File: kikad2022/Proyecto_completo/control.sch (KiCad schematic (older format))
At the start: 33 parts, among them IC2 LM393AD, IC3 74HC02PW,112, J1 Conn_01x02_Male, J10 Conn_01x01_Male, J2 Conn_01x01_Male, J4 Conn_01x01_Male, J5 Conn_01x01_Male, J6 Conn_01x01_Male, J7 Conn_01x01_Male, J9 Conn_01x01_Male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

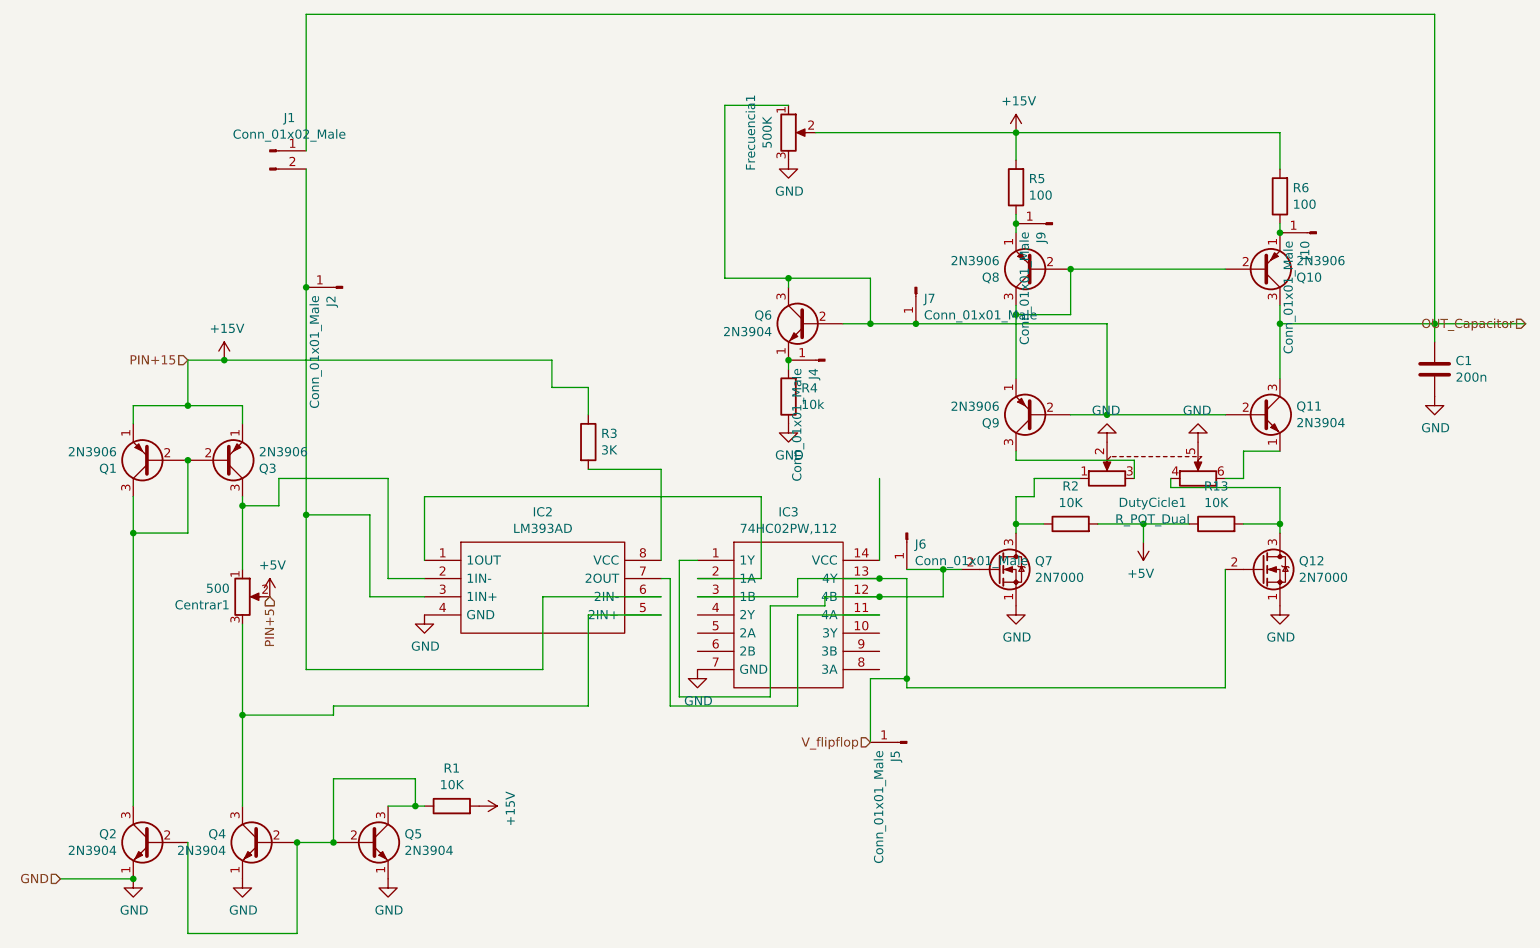
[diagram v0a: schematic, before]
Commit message: kikad_modificaciones
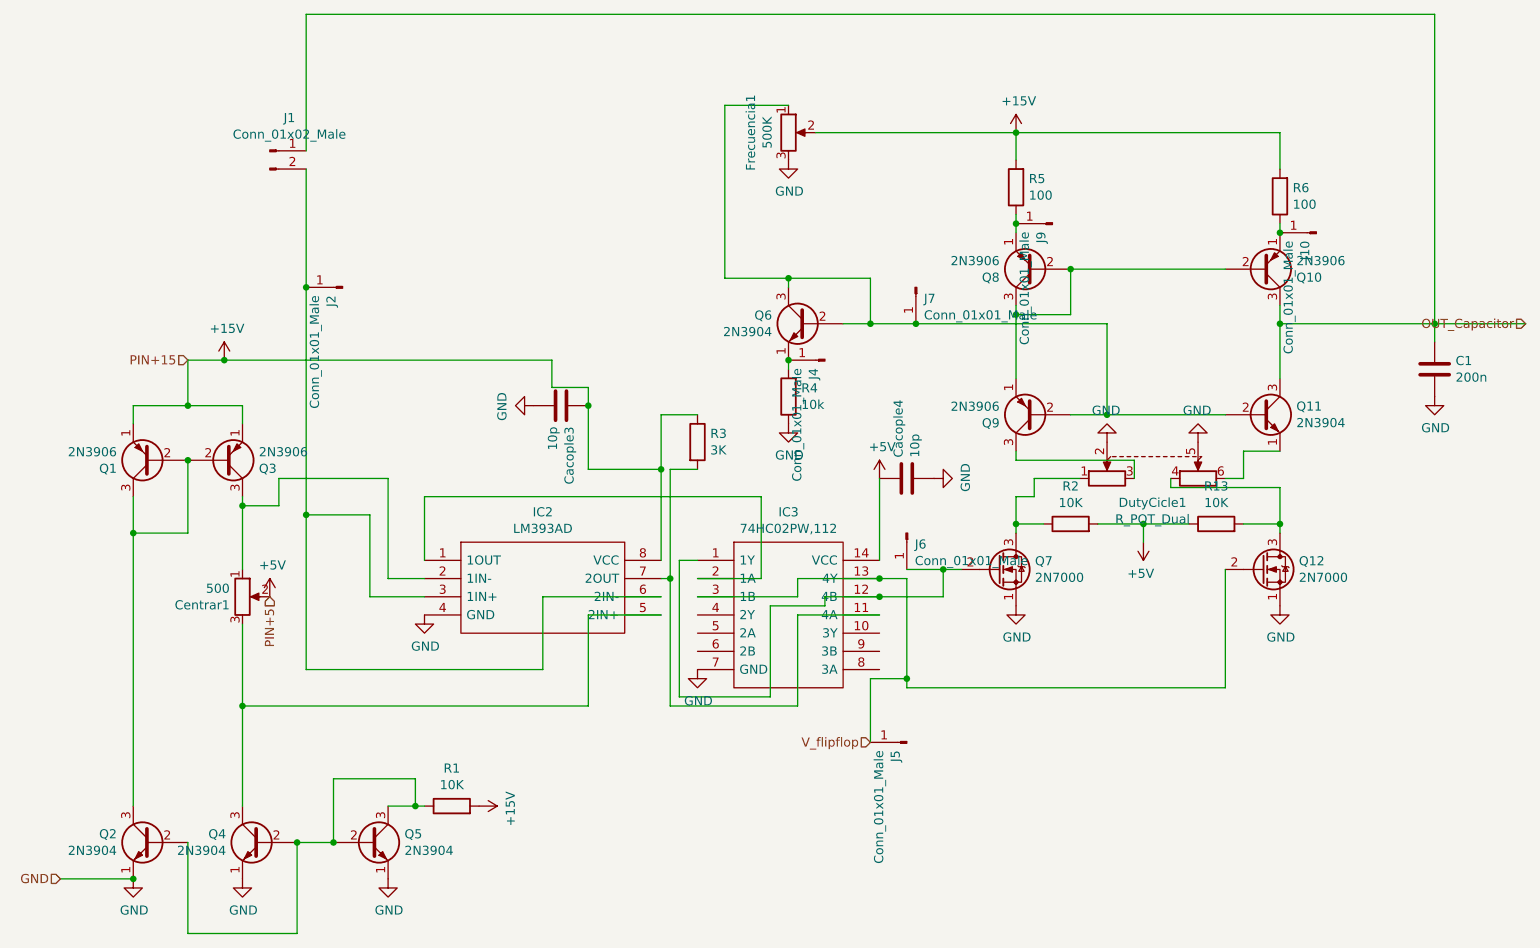
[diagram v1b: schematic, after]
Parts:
- added Cacople3, Cacople4: 10p, Capacitor_SMD:C_0603_1608Metric, symbol Device:C
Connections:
- net +15V: now also IC2.8 (VCC), Cacople3.2
- net +5V: now also IC3.14 (VCC), Cacople4.2
- net GND: now also Cacople3.1, Cacople4.1
- net at R3.2: now also IC2.7 (2OUT), IC3.11 (4A); no longer IC2.8 (VCC)
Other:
- moved on the sheet: R3
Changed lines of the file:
@@
 Connection ~ 3350 3850
 Connection ~ 3950 3700
-Wire Wire Line
-	3950 4850 4450 4850
-Wire Wire Line
-	4450 4850 4450 4800
 $Comp
 L Device:R R3
 U 1 1 61FADEA7
-P 5850 3350
-F 0 "R3" H 5920 3396 50  0000 L CNN
-F 1 "3K" H 5920 3305 50  0000 L CNN
-F 2 "Resistor_SMD:R_0603_1608Metric" V 5780 3350 50  0001 C CNN
-F 3 "~" H 5850 3350 50  0001 C CNN
-	1    5850 3350
+P 6450 3350
+F 0 "R3" H 6520 3396 50  0000 L CNN
+F 1 "3K" H 6520 3305 50  0000 L CNN
+F 2 "Resistor_SMD:R_0603_1608Metric" V 6380 3350 50  0001 C CNN
+F 3 "~" H 6450 3350 50  0001 C CNN
+	1    6450 3350
 	1    0    0    -1
 $EndComp
@@
 Connection ~ 10500 2700
 Wire Wire Line
-	5850 3050 5850 3200
+	5850 3050 5850 3150
 $Comp
 L power:+15V #PWR013
@@
 	1    0    0    -1
 $EndComp
-Connection ~ 3950 4850
-Wire Wire Line
-	3950 4850 3950 5350
+Connection ~ 3950 4800
+Wire Wire Line
+	3950 4800 3950 5350
 Connection ~ 4300 3750
 Wire Wire Line
@@
 	3950 3700 3950 4050
 Wire Wire Line
-	3950 4350 3950 4850
+	3950 4350 3950 4800
 $Comp
 L power:+5V #PWR016
@@
 Wire Wire Line
 	5850 4300 5850 4800
-Wire Wire Line
-	5850 4800 4450 4800
-Wire Wire Line
-	6250 4000 6250 3500
 Wire Wire Line
 	6250 3500 5850 3500
@@
 	6600 2450 6950 2450
 Connection ~ 6950 2450
+Wire Wire Line
+	3950 4800 5850 4800
+$Comp
+L power:+5V #PWR0107
+U 1 1 62601C7D
+P 7450 3550
+F 0 "#PWR0107" H 7450 3400 50  0001 C CNN
+F 1 "+5V" H 7465 3723 50  0000 C CNN
+F 2 "" H 7450 3550 50  0001 C CNN
+F 3 "" H 7450 3550 50  0001 C CNN
+	1    7450 3550
+	1    0    0    -1
+$EndComp
+$Comp
+L power:GND #PWR?
+U 1 1 6274CF4D
+P 7750 3550
+AR Path="/61FF2F62/6274CF4D" Ref="#PWR?"  Part="1"
+AR Path="/61F9DFF3/6274CF4D" Ref="#PWR028"  Part="1"
+F 0 "#PWR028" H 7750 3300 50  0001 C CNN
+F 1 "GND" H 7755 3377 50  0000 C CNN
+F 2 "" H 7750 3550 50  0001 C CNN
+F 3 "" H 7750 3550 50  0001 C CNN
+	1    7750 3550
+	0    -1   -1   0
+$EndComp
+$Comp
+L Device:C Cacople?
+U 1 1 6274CF53
+P 7600 3550
+AR Path="/61FF2F62/6274CF53" Ref="Cacople?"  Part="1"
+AR Path="/61F9DFF3/6274CF53" Ref="Cacople4"  Part="1"
+F 0 "Cacople4" H 7485 3504 50  0000 R CNN
+F 1 "10p" H 7485 3595 50  0000 R CNN
+F 2 "Capacitor_SMD:C_0603_1608Metric" H 7638 3400 50  0001 C CNN
+F 3 "~" H 7600 3550 50  0001 C CNN
+	1    7600 3550
+	0    1    1    0
+$EndComp
+$Comp
+L power:GND #PWR?
+U 1 1 627525A4
+P 5550 3150
+AR Path="/61FF2F62/627525A4" Ref="#PWR?"  Part="1"
+AR Path="/61F9DFF3/627525A4" Ref="#PWR027"  Part="1"
+F 0 "#PWR027" H 5550 2900 50  0001 C CNN
+F 1 "GND" H 5555 2977 50  0000 C CNN
+F 2 "" H 5550 3150 50  0001 C CNN
+F 3 "" H 5550 3150 50  0001 C CNN
+	1    5550 3150
+	0    1    1    0
+$EndComp
+$Comp
+L Device:C Cacople?
+U 1 1 627525AA
+P 5700 3150
+AR Path="/61FF2F62/627525AA" Ref="Cacople?"  Part="1"
+AR Path="/61F9DFF3/627525AA" Ref="Cacople3"  Part="1"
+F 0 "Cacople3" H 5585 3104 50  0000 R CNN
+F 1 "10p" H 5585 3195 50  0000 R CNN
+F 2 "Capacitor_SMD:C_0603_1608Metric" H 5738 3000 50  0001 C CNN
+F 3 "~" H 5700 3150 50  0001 C CNN
+	1    5700 3150
+	0    -1   -1   0
+$EndComp
+Connection ~ 5850 3150
+Wire Wire Line
+	6250 3500 6250 4000
+Wire Wire Line
+	5850 3150 5850 3500
+Wire Wire Line
+	6450 3200 6250 3200
+Wire Wire Line
+	6250 3200 6250 3500
+Connection ~ 6250 3500
+Wire Wire Line
+	6300 3500 6450 3500
+Wire Wire Line
+	6300 3500 6300 4100
+Connection ~ 6300 4100
 $EndSCHEMATC
